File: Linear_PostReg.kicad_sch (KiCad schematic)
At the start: 42 parts, among them Q301 MMBT3904, Q302 TIP42C, Q303 BSS138, Q304 MMBT3904, U301 TLV4387PWR, U302 LMV331

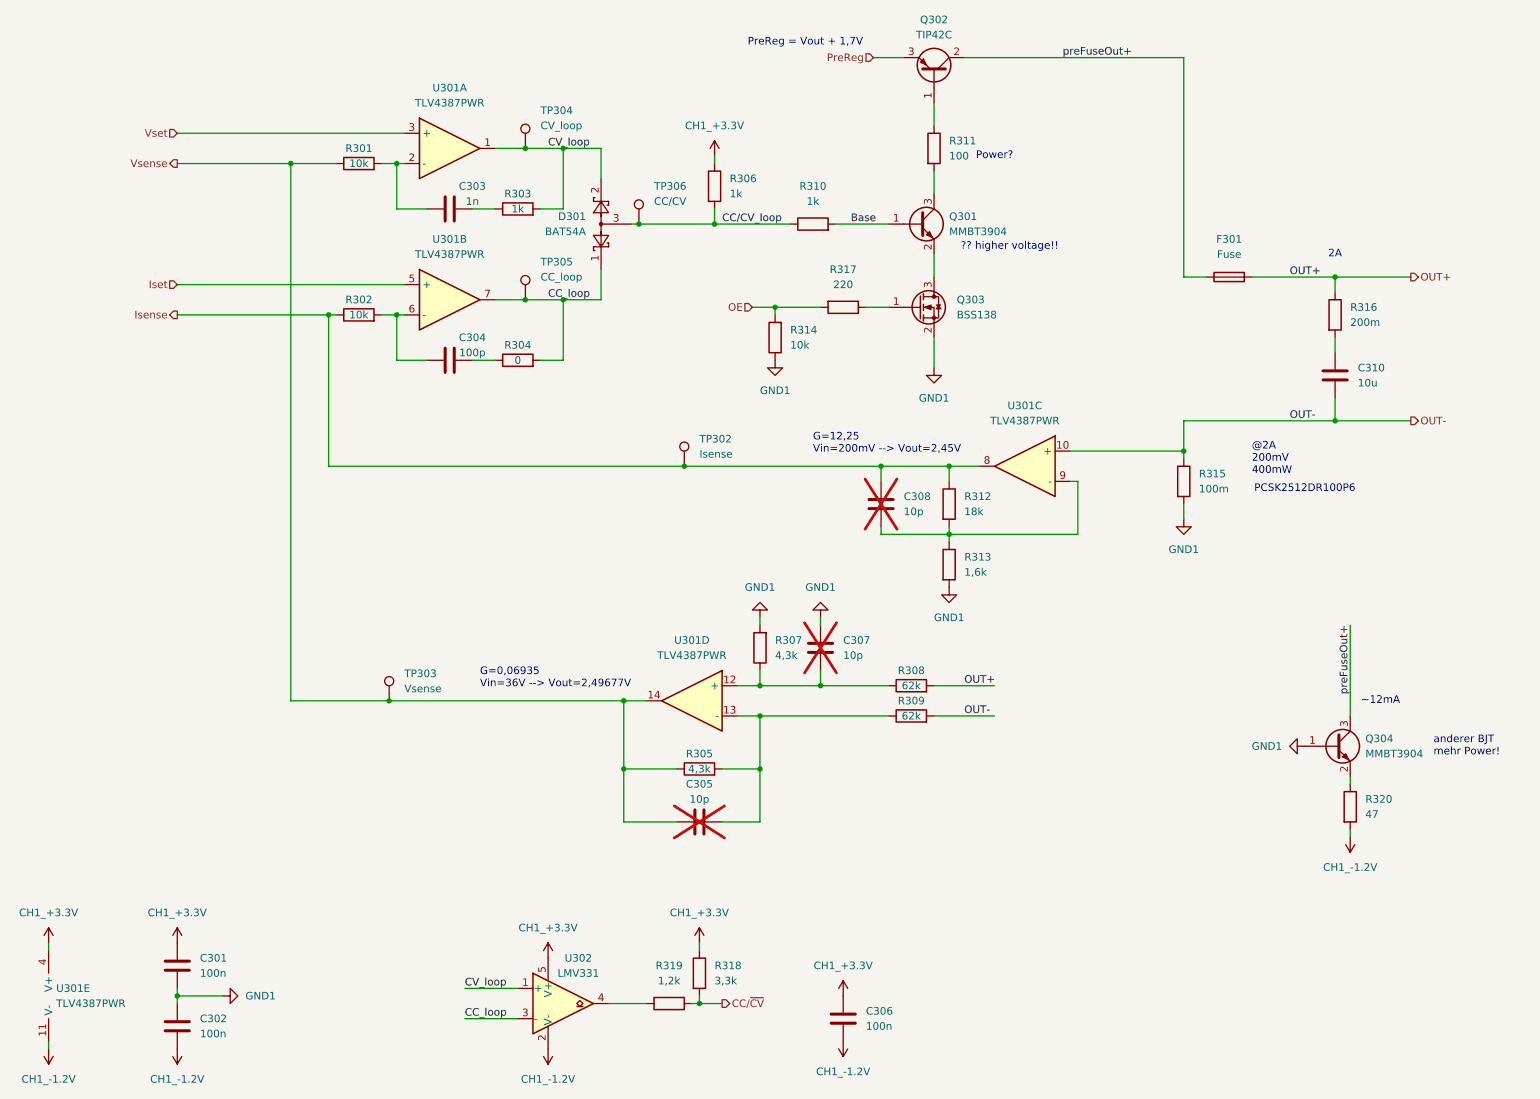
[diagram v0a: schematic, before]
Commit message: changed pass element drive
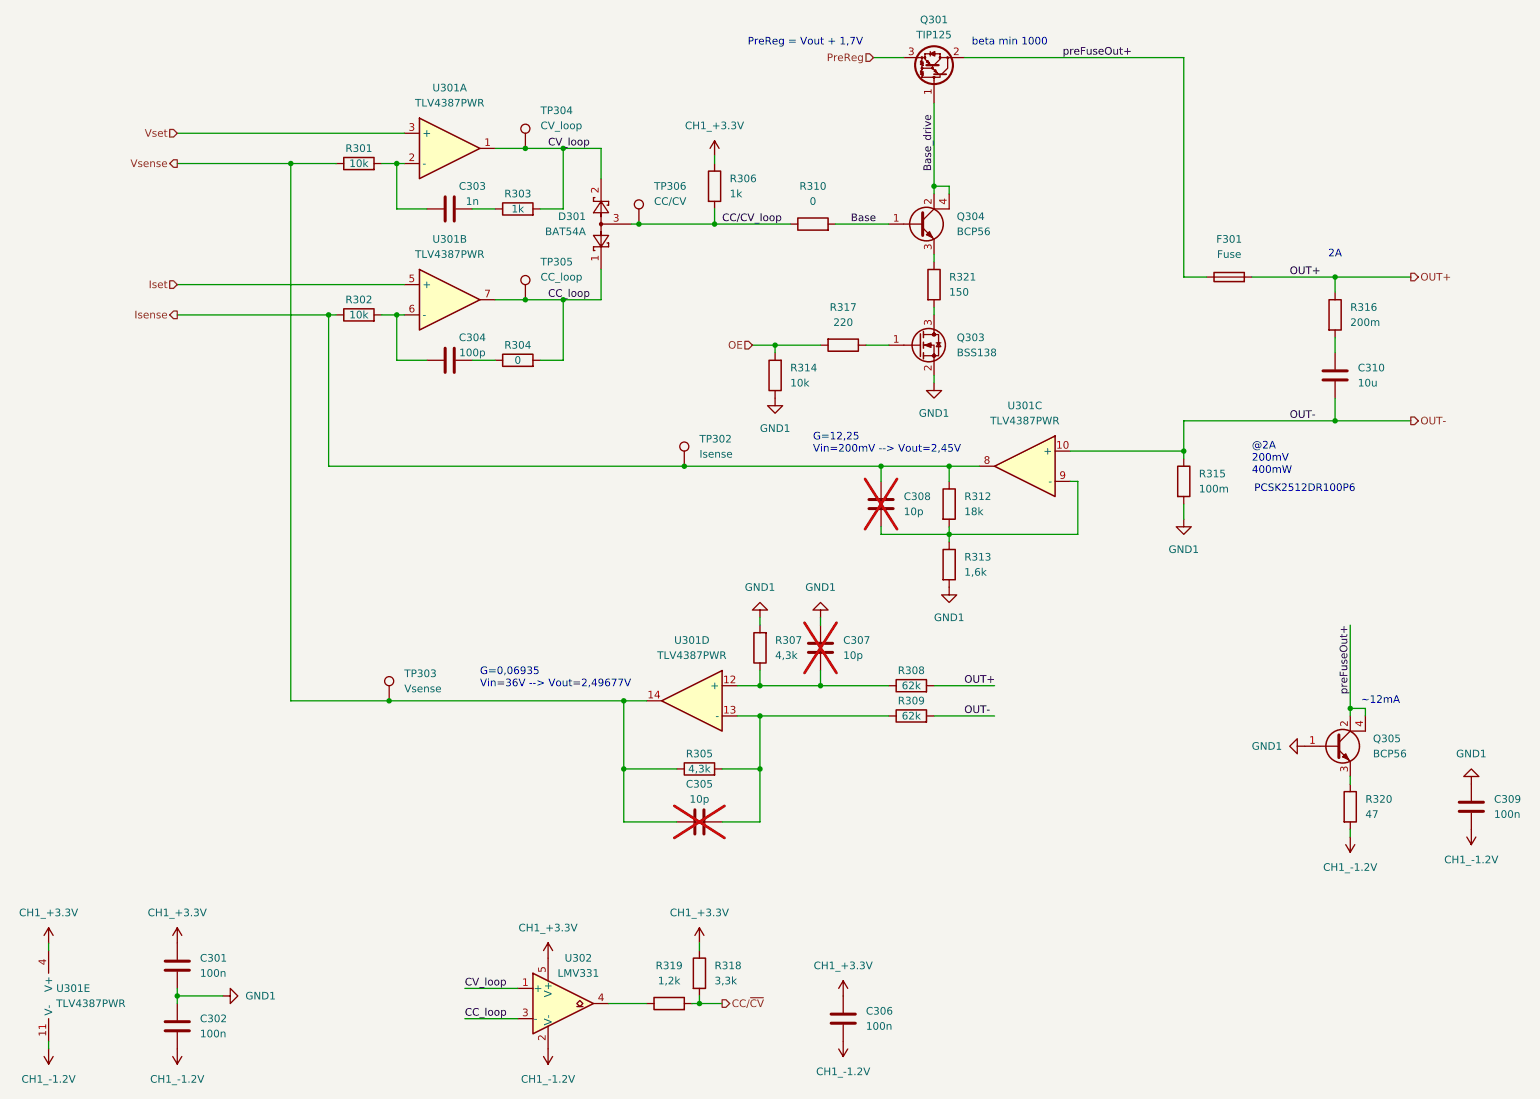
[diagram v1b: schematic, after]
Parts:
- removed Q301, Q304: MMBT3904, Package_TO_SOT_SMD:SOT-23-3, symbol Transistor_BJT:MMBT3904
- removed Q302: TIP42C, Package_TO_SOT_THT:TO-220-3_Horizontal_TabUp, symbol Transistor_BJT:TIP42C
- removed R311: 100, Resistor_SMD:R_0603_1608Metric, symbol Device:R
- added C309: 100n, Capacitor_SMD:C_0603_1608Metric, symbol Device:C
- added Q301: TIP125, Package_TO_SOT_THT:TO-220-3_Horizontal_TabUp, symbol Transistor_BJT:TIP125
- added Q304, Q305: BCP56, Package_TO_SOT_SMD:SOT-223, symbol Transistor_BJT:BCP56
- added R321: 150, Resistor_SMD:R_1206_3216Metric, symbol Device:R
- R310: value 1k -> 0
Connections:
- net Base: now also Q304.1 (B)
- net CH1_-1.2V: now also C309.2
- net GND1: now also C309.1, Q305.1 (B)
- net PreReg: now also Q301.3 (E)
- net preFuseOut+: now also Q301.2 (C), Q305.2 (C), Q305.4 (C)
- net at Q303.3 (D): now also R321.2
- net at R320.1: now also Q305.3 (E)
- new net: Q304.3 (E), R321.1
- new net Base_drive: Q301.1 (B), Q304.2 (C), Q304.4 (C)
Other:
- note added: "beta min 1000"
- note removed: "?? higher voltage!!"
- note removed: "Power?"
- note removed: "anderer BJT mehr Power!"
- moved on the sheet: Q303, R314, R317
